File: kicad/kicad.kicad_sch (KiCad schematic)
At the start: 0 parts

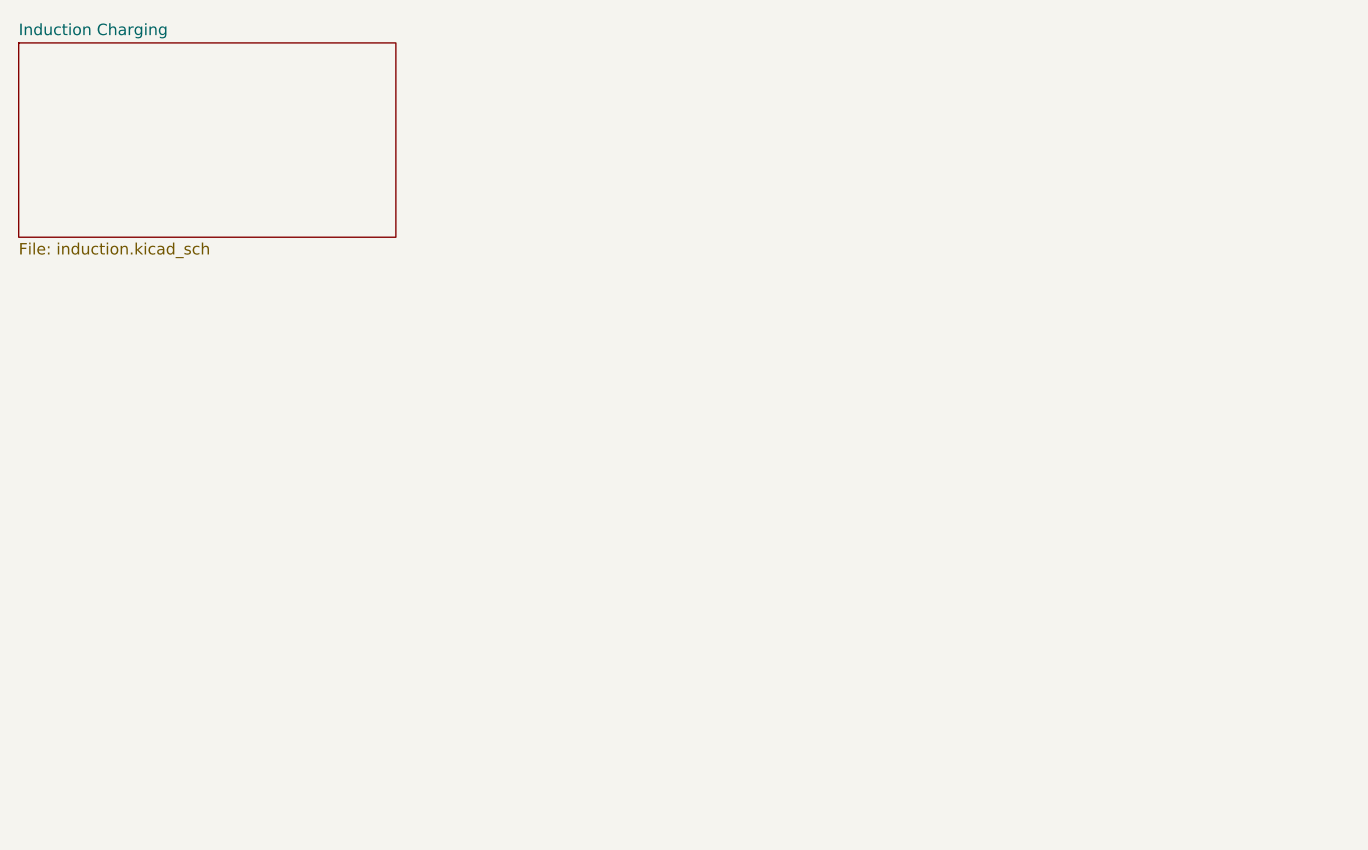
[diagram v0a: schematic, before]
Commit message: Update induction charging schematic
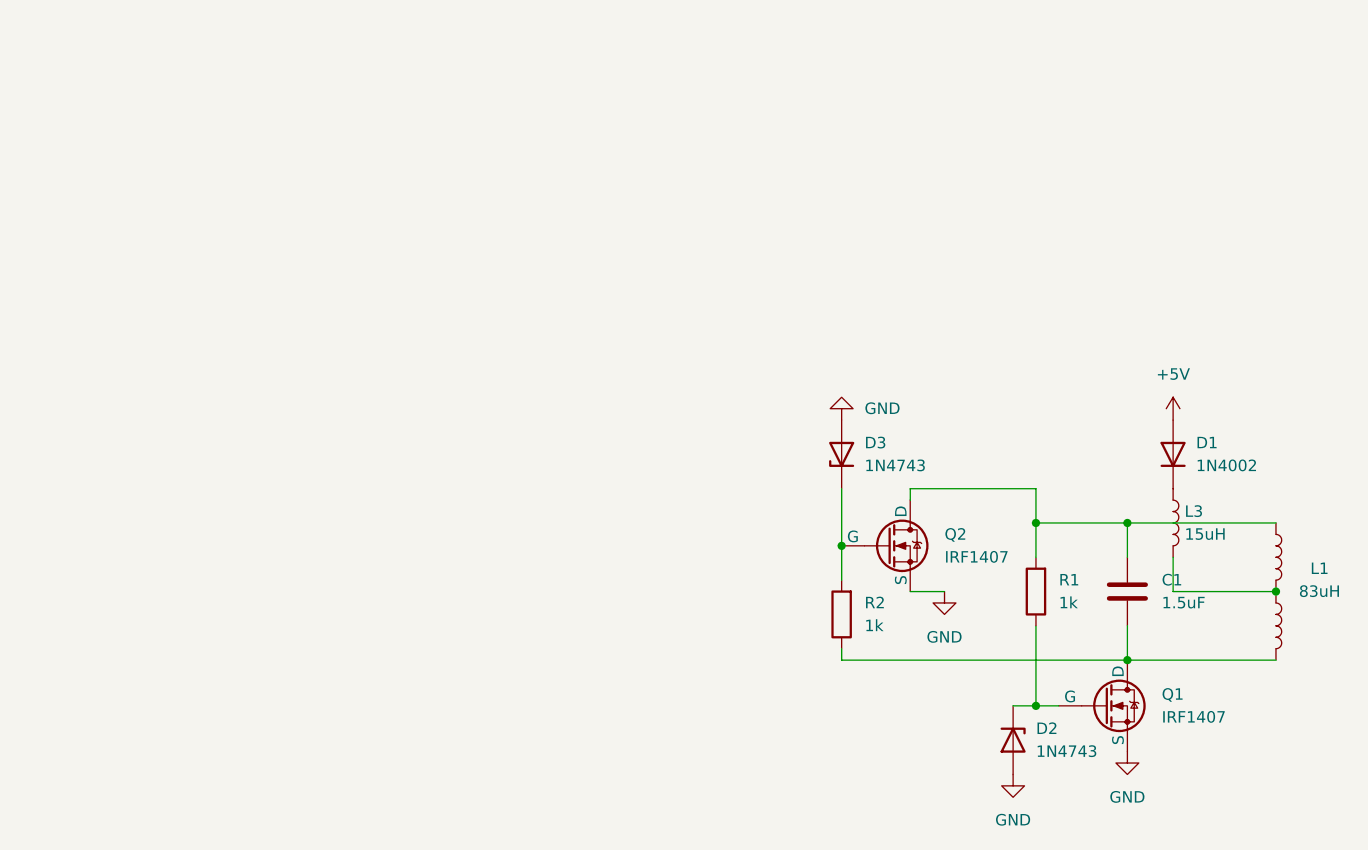
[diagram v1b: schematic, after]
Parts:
- added C1: 1.5uF, symbol Device:C
- added D1: 1N4002, Diode_THT:D_DO-41_SOD81_P10.16mm_Horizontal, symbol Diode:1N4002
- added D2, D3: 1N4743, Diode_THT:D_DO-41_SOD81_P10.16mm_Horizontal, symbol Diode:1N47xxA
- added L1: 83uH, symbol Device:L
- added L2: L, symbol Device:L
- added L3: 15uH, symbol Device:L
- added Q1, Q2: IRF1407, symbol Simulation_SPICE:NMOS
- added R1, R2: 1k, symbol Device:R
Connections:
- new net: D2.1 (K), Q1.2 (G), R1.1
- new net: C1.1, L1.1, Q2.1 (D), R1.2
- new net: D1.1 (K), L3.1
- new net: C1.2, L2.2, Q1.1 (D), R2.1
- new net: L1.2, L2.1, L3.2
- new net: D3.1 (K), Q2.2 (G), R2.2
- new net +5V: D1.2 (A)
- new net GND: D2.2 (A), D3.2 (A), Q1.3 (S), Q2.3 (S)
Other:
- removed sheet Induction Charging
- title: (none) -> Induction charging transmitter circuit
